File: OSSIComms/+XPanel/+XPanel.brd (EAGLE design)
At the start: 109.5 x 83 mm, 19 parts, among them X1 RFCON-MCX-V, X10 P-PAD, X11 P-PAD-S, X2 RFCON-MCX-V, X3 P-PAD-S, X4 P-PAD-S, X5 P-PAD-S, X6 P-PAD, X7 P-PAD, X8 P-PAD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

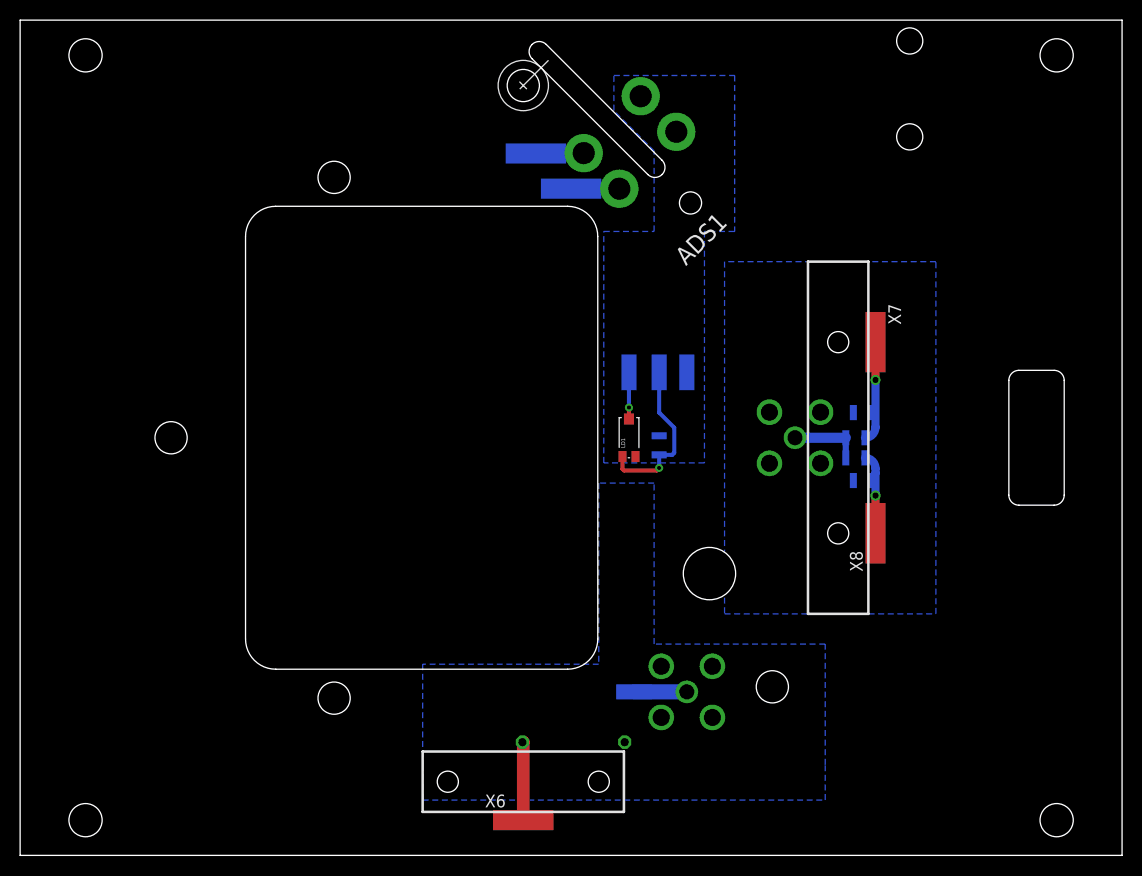
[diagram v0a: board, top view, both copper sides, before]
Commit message: +Xpanel size changed
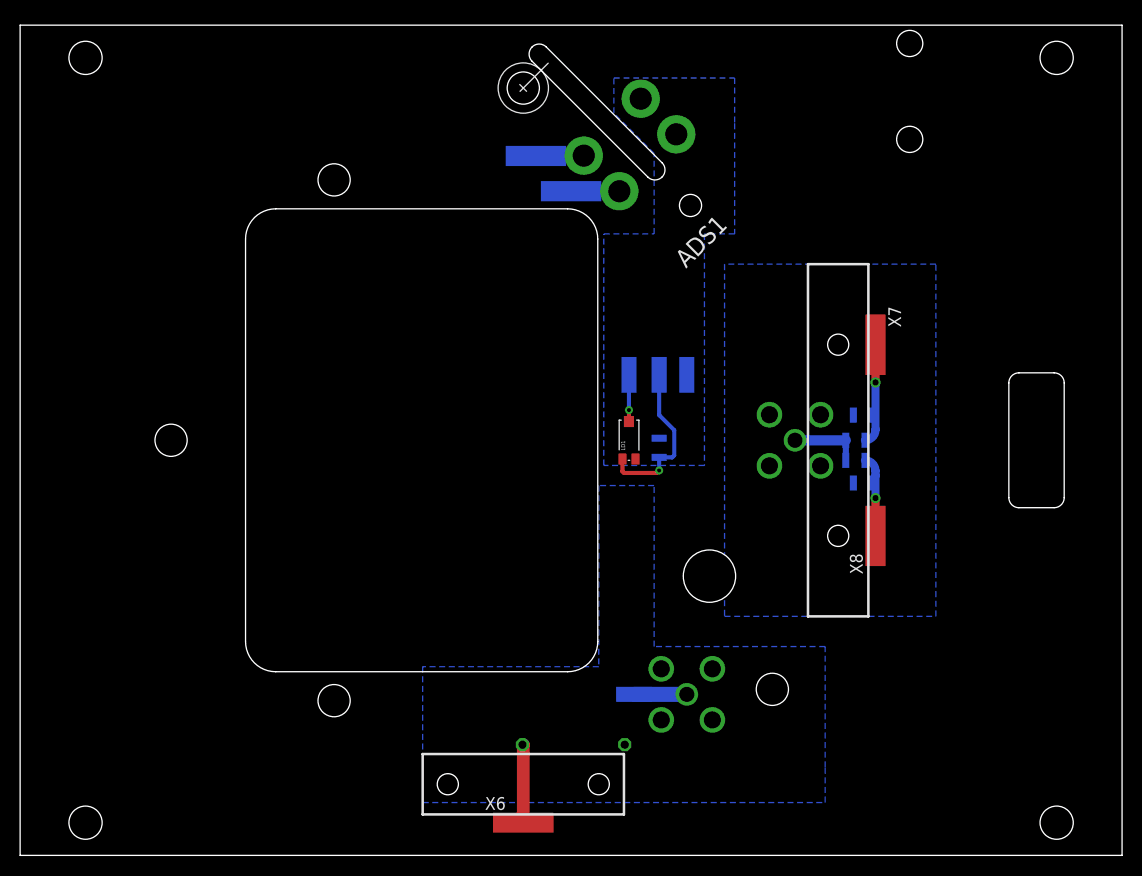
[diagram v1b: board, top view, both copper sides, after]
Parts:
- moved ADS1 0.25 mm to (50.0, 76.2)
- moved C1 0.25 mm to (83.0, 41.2)
- moved C2 0.25 mm to (83.8, 37.0)
- moved L1 0.25 mm to (83.0, 39.2)
- moved L2 0.25 mm to (83.8, 43.8)
- moved L3 0.25 mm to (55.0, 11.0)
- moved LD1 0.25 mm to (60.5, 41.2)
- moved R1 0.25 mm to (63.5, 40.5)
- moved X1 0.25 mm to (66.2, 16.0)
- moved X10 0.25 mm to (54.8, 66.0)
- moved X11 0.25 mm to (61.0, 16.0)
- moved X2 0.25 mm to (77.0, 41.2)
- moved X3 0.25 mm to (66.2, 47.8)
- moved X4 0.25 mm to (63.5, 47.8)
- moved X5 0.25 mm to (60.5, 47.8)
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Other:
- board size 109.5 x 83 mm -> 109.5 x 82.5 mm
